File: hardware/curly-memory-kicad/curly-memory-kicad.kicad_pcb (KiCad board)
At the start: 2 copper layers, 30 x 100.5 mm, 138 parts, among them J101 Conn_01x05, J102 Conn_01x05, J103 Conn_01x01_Male, J104 Conn_01x01_Male, J105 Conn_01x01_Male, J106 Conn_01x01_Male, J107 AudioJack2, J201 AudioJack2, J202 AudioJack2, J203 AudioJack2, J204 Conn_01x01_Male, J205 Conn_01x01_Male, J206 Conn_01x01_Male, J207 Conn_01x01_Male, J301 Conn_01x01_Male, J302 Conn_01x01_Male, J303 Conn_01x01_Male, J304 Conn_01x01_Male, J305 AudioJack2, J306 AudioJack2, J307 AudioJack2, J308 AudioJack2, J501 Conn_02x05_Odd_Even, SW101 FSM, SW102 FSM, SW401 FSM, SW402 FSM, U101 MCP3008-I/SL, U102 ESP32-WROOM-32, U103 MCP4822-E/SN, U104 MCP4822-E/SN, U105 MCP42010-E/SL, U106 MCP42010-E/SL, U107 MCP6004, U201 MCP6004, U301 MCP6004, U501 NCP1117-5.0_SOT223, U502 NCP1117-3.3_SOT223

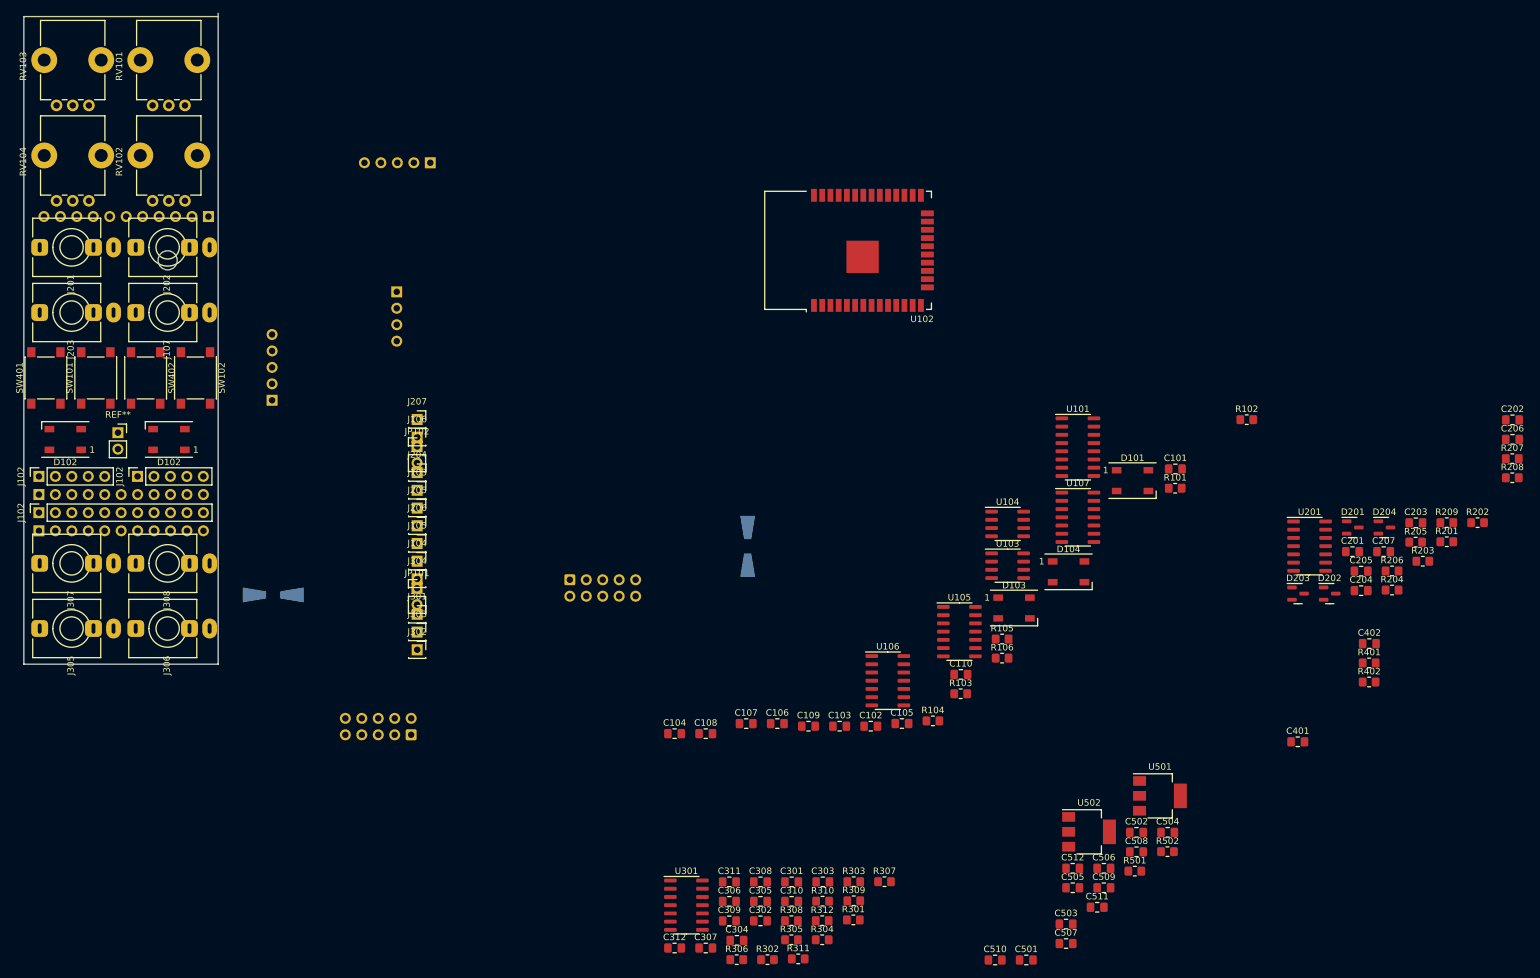
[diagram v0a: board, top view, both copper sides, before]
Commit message: all components placed on the main board
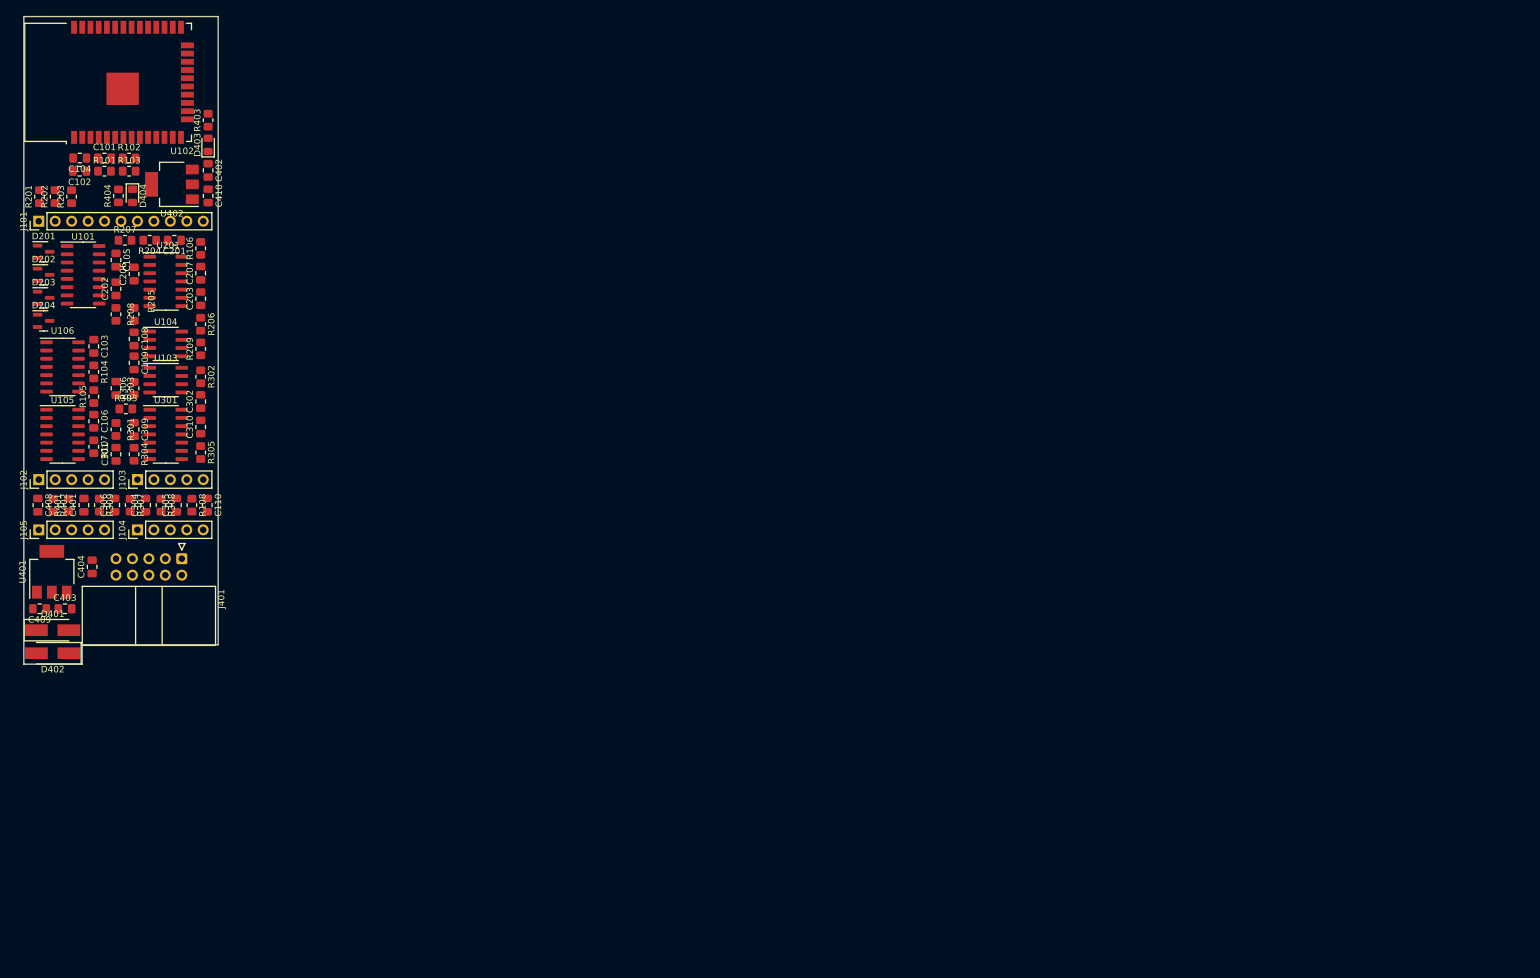
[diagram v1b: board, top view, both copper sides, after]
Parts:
- removed C107, C204, C205, C307, C308, C502, C503, C504, C509, C510: 1uF, Capacitor_SMD:C_0805_2012Metric_Pad1.18x1.45mm_HandSolder
- removed C311, C312, C501, C505, C506, C507, C508, C511, C512: 100nF, Capacitor_SMD:C_0805_2012Metric_Pad1.18x1.45mm_HandSolder
- removed D101, D102 (x2), D103, D104: WS2812B, LED_SMD:LED_WS2812B_PLCC4_5.0x5.0mm_P3.2mm
- removed D501, D502: S1A, Diode_SMD:D_SMA-SMB_Universal_Handsoldering
- removed the J101 at (28.5, 30.9)
- removed the J101 at (38.3, 59.2)
- removed the J102 at (17.6, 71.0)
- removed the J102 at (2.33, 76.6)
- removed the J102 at (2.33, 71.0)
- removed the J102 at (2.33, 79.4)
- removed the J102 at (2.33, 73.8)
- removed the J102 at (62.8, 22.6)
- removed J106, J204, J205, J206, J207, J301, J302, J303, J304: Conn_01x01_Male, Connector_PinSocket_2.54mm:PinSocket_1x01_P2.54mm_Vertical
- removed J107, J201, J202, J203, J305, J306, J307, J308: AudioJack2, AudioJacks:Jack_3.5mm_QingPu_WQP-PJ398SM_Vertical
- removed J501: Conn_02x05_Odd_Even, Connector_IDC:IDC-Header_2x05_P2.54mm_Vertical
- removed JP101, JP102: Jumper_2_Open, Connector_PinHeader_2.54mm:PinHeader_1x02_P2.54mm_Vertical
- removed R310, R311, R312, R501: 100K, Resistor_SMD:R_0805_2012Metric_Pad1.20x1.40mm_HandSolder
- removed R502: 56k, Resistor_SMD:R_0805_2012Metric_Pad1.20x1.40mm_HandSolder
- removed REF**: PinSocket_1x02_P2.54mm_Vertical, Connector_PinSocket_2.54mm:PinSocket_1x02_P2.54mm_Vertical
- removed REF**: IDC-Header_2x05_P2.54mm_Horizontal, Connector_IDC:IDC-Header_2x05_P2.54mm_Horizontal
- removed REF**: PinSocket_1x04_P2.54mm_Vertical, Connector_PinSocket_2.54mm:PinSocket_1x04_P2.54mm_Vertical
- removed RV101, RV102, RV103, RV104: PTV09A-4225F-B203, Potentiometer_THT:Potentiometer_Bourns_PTV09A-1_Single_Vertical
- removed SW101, SW102, SW401, SW402: FSM, Button_Switch_SMD:SW_Push_1P1T_NO_6x6mm_H9.5mm
- removed U107: MCP6004, Package_SO:SOIC-14_3.9x8.7mm_P1.27mm
- removed U501: NCP1117-5.0_SOT223, Package_TO_SOT_SMD:SOT-223-3_TabPin2
- removed U502: NCP1117-3.3_SOT223, Package_TO_SOT_SMD:SOT-223-3_TabPin2
- added C403: 10uF, Capacitor_SMD:C_0805_2012Metric_Pad1.18x1.45mm_HandSolder, F.Cu at (6.35, 91.4)
- added C404: 10uF, Capacitor_SMD:C_0805_2012Metric_Pad1.18x1.45mm_HandSolder, F.Cu at (10.5, 85.0)
- added C408: 100nF, Capacitor_SMD:C_0805_2012Metric_Pad1.18x1.45mm_HandSolder, F.Cu at (2.16, 75.4)
- added C409: 10uF, Capacitor_SMD:C_0805_2012Metric_Pad1.18x1.45mm_HandSolder, F.Cu at (2.43, 91.4)
- added C410: 10uF, Capacitor_SMD:C_0805_2012Metric_Pad1.18x1.45mm_HandSolder, F.Cu at (28.4, 27.7)
- added D401: S1A, Diode_SMD:D_SMA_Handsoldering, F.Cu at (4.45, 94.7)
- added D402: S1A, Diode_SMD:D_SMA_Handsoldering, F.Cu at (4.45, 98.3)
- added D403: LED, LED_SMD:LED_0805_2012Metric_Pad1.15x1.40mm_HandSolder, F.Cu at (28.4, 19.8)
- added D404: LED, LED_SMD:LED_0805_2012Metric_Pad1.15x1.40mm_HandSolder, F.Cu at (16.8, 27.7)
- added J101: Conn_01x11, Connector_PinHeader_2.54mm:PinHeader_1x11_P2.54mm_Vertical, F.Cu at (2.30, 31.6)
- added J102: Conn_01x05, Connector_PinHeader_2.54mm:PinHeader_1x05_P2.54mm_Vertical, F.Cu at (2.30, 71.5)
- added J401: Conn_02x05_Odd_Even, Connector_IDC:IDC-Header_2x05_P2.54mm_Horizontal, F.Cu at (24.4, 83.7)
- added R107: 100R, Resistor_SMD:R_0805_2012Metric_Pad1.20x1.40mm_HandSolder, F.Cu at (10.8, 66.4)
- added R108: 100K, Resistor_SMD:R_0805_2012Metric_Pad1.20x1.40mm_HandSolder, F.Cu at (25.9, 75.4)
- added R403: 150R, Resistor_SMD:R_0805_2012Metric_Pad1.20x1.40mm_HandSolder, F.Cu at (28.4, 16.0)
- added R404: 150R, Resistor_SMD:R_0805_2012Metric_Pad1.20x1.40mm_HandSolder, F.Cu at (14.6, 27.7)
- added U401: NCP1117-5.0_SOT223, Package_TO_SOT_SMD:SOT-223-3_TabPin2, F.Cu at (4.32, 85.7)
- added U402: NCP1117-3.3_SOT223, Package_TO_SOT_SMD:SOT-223-3_TabPin2, F.Cu at (22.9, 25.9)
- C103, C106, C309, C310: value 1uF -> 100nF
- C304: value 22pF -> 1uF
- C402: value 100nF -> 10uF
- J103, J104, J105: value Conn_01x01_Male -> Conn_01x05; footprint Connector_PinSocket_2.54mm:PinSocket_1x01_P2.54mm_Vertical -> Connector_PinHeader_2.54mm:PinHeader_1x05_P2.54mm_Vertical
- R105: value 100R -> 1K
- R106: value 100K -> 1K
- R304: value 47k -> 100K
- R401: value 1K -> 100K
- R402: value 1K -> 56k
- moved R202 225.3 mm to (4.83, 27.8), turned to 90 degrees
- moved R201 223.7 mm to (2.41, 27.8), turned to 90 degrees
- moved R208 217.1 mm to (14.2, 46.0), turned to -90 degrees
- moved R207 216.8 mm to (15.6, 34.5)
- moved C202 216.6 mm to (14.2, 42.0), turned to 90 degrees
- moved R203 216.1 mm to (7.37, 27.8), turned to 90 degrees
- moved C206 214.4 mm to (17.0, 39.8), turned to 90 degrees
- moved D204 209.5 mm to (3.05, 47.0)
- moved D201 206.6 mm to (3.05, 36.3)
- moved R402 205.0 mm to (4.54, 75.4), turned to -90 degrees
- moved D202 204.6 mm to (3.05, 39.9)
- moved R401 202.3 mm to (6.89, 75.4), turned to 90 degrees
- moved R205 201.0 mm to (17.0, 46.0), turned to -90 degrees
- moved R204 199.3 mm to (19.4, 34.5), turned to 180 degrees
- moved D203 199.0 mm to (3.05, 43.4)
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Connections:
- C102 pad 1: +5V -> +3V3
- C103 pad 1: +3V3 -> +5V
- C104 pad 1: +5V -> +3V3
- C105 pad 1: +3V3 -> +5V
- C110 pad 2: Net-(C110-Pad2) -> /DRY_WET
- C304 pad 1: Net-(C304-Pad1) -> /output/OUT_1_OUT
- C304 pad 2: Net-(C304-Pad2) -> Net-(C301-Pad1)
- C305 pad 1: /output/OUT_1 -> /output/OUT_2_OUT
- C305 pad 2: Net-(C301-Pad1) -> Net-(C302-Pad1)
- C306 pad 1: /output/OUT_2 -> /output/OUT_0_OUT
- C306 pad 2: Net-(C302-Pad1) -> Net-(C303-Pad1)
- C401 pad 1: GND -> +5V
- C402 pad 1: GND -> +5V
- J103 pad 1: /RES0_A1 -> Net-(J103-Pad1)
- J104 pad 1: /RES0_W1 -> /output/OUT_0_OUT
- J105 pad 1: GND -> /RES0_A1
- R102 pad 1: /RES1_W0 -> +3V3
- R102 pad 2: Net-(R102-Pad2) -> /SW_1
- R103 pad 1: /RES1_W1 -> +3V3
- R103 pad 2: Net-(R102-Pad2) -> /SW_0
- R104 pad 1: Net-(R102-Pad2) -> /RES1_W0
- R105 pad 1: Net-(R104-Pad2) -> /RES1_W1
- R105 pad 2: /RES0_A1 -> Net-(R104-Pad2)
- R106 pad 1: GND -> Net-(R104-Pad2)
- R106 pad 2: Net-(C110-Pad2) -> Net-(R106-Pad2)
- R201 pad 1: Net-(J201-PadS) -> /input/IN_0_IN+
- R202 pad 1: Net-(J202-PadS) -> /input/IN_1_IN+
- R203 pad 1: Net-(J203-PadS) -> /input/IN_2_IN+
- R303 pad 1: /output/OUT_3+ -> /output/OUT_0+
- R304 pad 1: /output/OUT_0+ -> Net-(C301-Pad2)
- R304 pad 2: Net-(C304-Pad2) -> Net-(C301-Pad1)
- R305 pad 1: Net-(C301-Pad2) -> Net-(C302-Pad2)
- R305 pad 2: Net-(C301-Pad1) -> Net-(C302-Pad1)
- R306 pad 1: Net-(C302-Pad2) -> Net-(C303-Pad2)
- R306 pad 2: Net-(C302-Pad1) -> Net-(C303-Pad1)
- R307 pad 1: Net-(C303-Pad2) -> GND
- R307 pad 2: Net-(C303-Pad1) -> /output/OUT_1_OUT
- R308 pad 1: Net-(C304-Pad2) -> GND
- R308 pad 2: Net-(C304-Pad1) -> /output/OUT_2_OUT
- R309 pad 2: /output/OUT_1 -> /output/OUT_0_OUT
- R401 pad 1: +3V3 -> +5V
- R401 pad 2: /SW_0 -> V_OFFSET
- R402 pad 1: +3V3 -> V_OFFSET
- R402 pad 2: /SW_1 -> GND
- U102 pad 10: Net-(J102-Pad5) -> unconnected-(U102-Pad10)
- U102 pad 24: Net-(J102-Pad1) -> unconnected-(U102-Pad24)
- U102 pad 28: Net-(J102-Pad2) -> Net-(J103-Pad1)
- U102 pad 33: Net-(J102-Pad3) -> unconnected-(U102-Pad33)
- U102 pad 36: Net-(J102-Pad4) -> unconnected-(U102-Pad36)
- U102 pad 8: unconnected-(U102-Pad8) -> Net-(U102-Pad8)
- U201 pad 12: (no net) -> GND
- U201 pad 13: (no net) -> Net-(R104-Pad2)
- U201 pad 14: (no net) -> Net-(R106-Pad2)
- U301 pad 1: Net-(C304-Pad1) -> Net-(C303-Pad1)
- U301 pad 12: GND -> unconnected-(U301-Pad12)
- U301 pad 13: Net-(C303-Pad2) -> unconnected-(U301-Pad13)
- U301 pad 14: Net-(C303-Pad1) -> unconnected-(U301-Pad14)
- U301 pad 2: Net-(C304-Pad2) -> Net-(C303-Pad2)
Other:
- board size 30 x 100.5 mm -> 30 x 100 mm

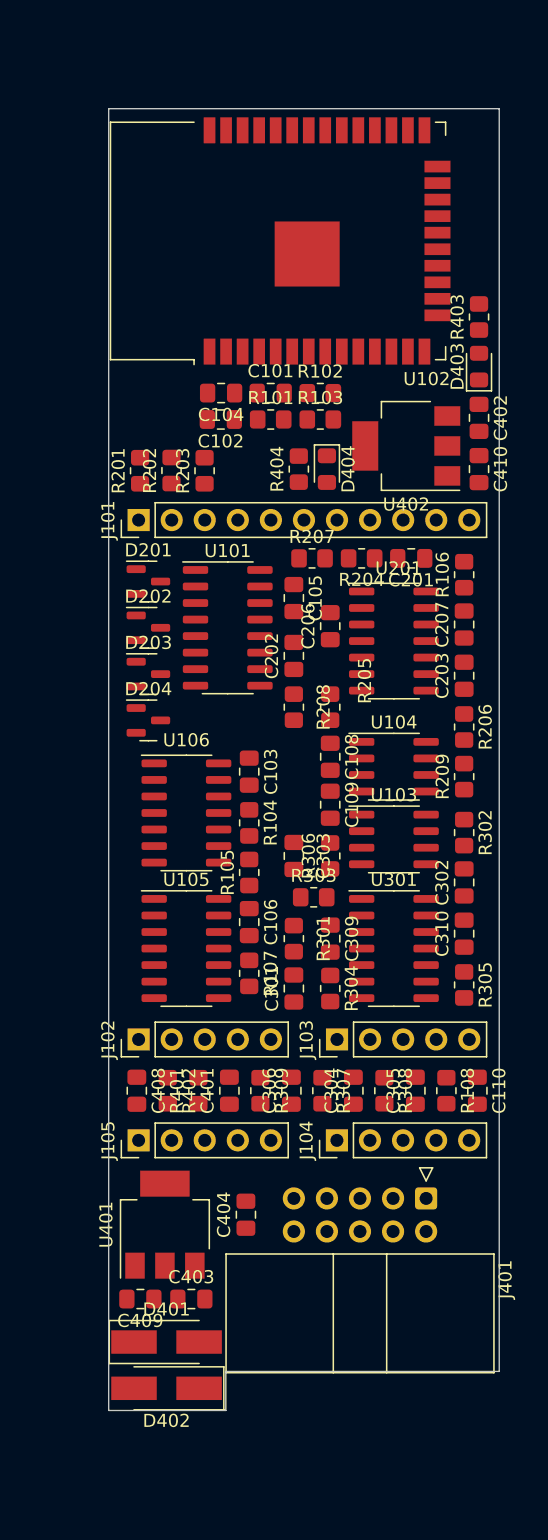
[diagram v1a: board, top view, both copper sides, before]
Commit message: more pcb tracked
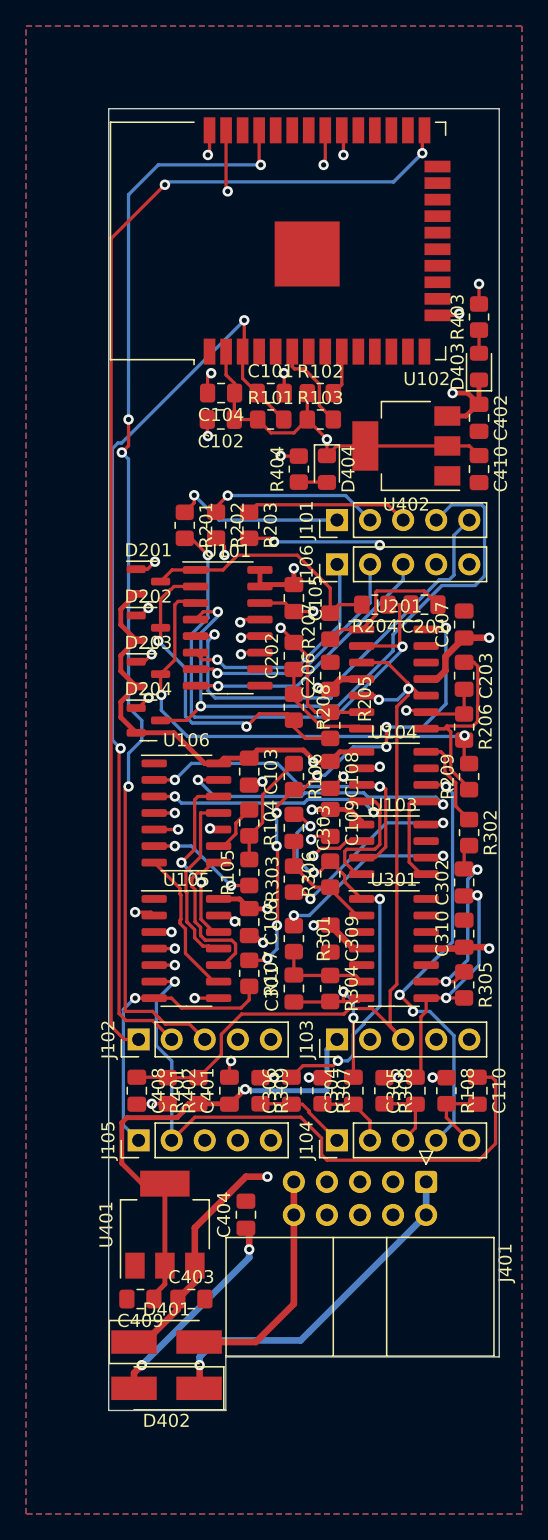
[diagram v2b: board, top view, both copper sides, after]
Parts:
- added J106: Conn_01x05, Connector_PinHeader_2.54mm:PinHeader_1x05_P2.54mm_Vertical, F.Cu at (17.5, 35.0)
- J101: value Conn_01x11 -> Conn_01x06; footprint Connector_PinHeader_2.54mm:PinHeader_1x11_P2.54mm_Vertical -> Connector_PinHeader_2.54mm:PinHeader_1x05_P2.54mm_Vertical
- moved R106 20.3 mm to (14.2, 51.3), turned to -90 degrees
- moved J101 15.2 mm to (17.5, 31.6)
- moved R201 5.42 mm to (5.84, 32.0), turned to -90 degrees
- moved R202 5.42 mm to (8.26, 32.0), turned to -90 degrees
- moved R203 5.42 mm to (10.8, 32.0), turned to -90 degrees
- moved R207 5.39 mm to (17.0, 39.8), turned to 90 degrees
- moved C206 3.81 mm to (17.0, 43.6)
- moved C201 3.70 mm to (24.3, 38.1)
- moved R204 3.70 mm to (20.4, 38.1)
- moved U201 2.92 mm to (21.9, 43.8)
- moved C303 2.16 mm to (14.2, 55.2)
- moved R303 2.07 mm to (14.2, 59.2), turned to 90 degrees
- moved R205 1.40 mm to (17.0, 47.4)
- moved C108 1.40 mm to (17.0, 51.2)
- moved C109 1.40 mm to (17.0, 54.9)
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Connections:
- J103 pad 1: Net-(J103-Pad1) -> +5V
- J103 pad 2: Net-(U102-Pad8) -> +3V3
- J103 pad 4: +3V3 -> Net-(J103-Pad4)
- J103 pad 5: +5V -> Net-(U102-Pad33)
- U102 pad 10: unconnected-(U102-Pad10) -> /RES_~SHDN
- U102 pad 11: unconnected-(U102-Pad11) -> /RES_~RS
- U102 pad 28: Net-(J103-Pad1) -> /SPI2_CS_2
- U102 pad 33: unconnected-(U102-Pad33) -> Net-(U102-Pad33)
- U102 pad 8: Net-(U102-Pad8) -> Net-(J103-Pad4)
- U104 pad 2: /SPI3_CS_1 -> /SPI2_CS_1
- U104 pad 3: /SPI3_CLK -> /SPI2_CLK
- U104 pad 4: /SPI3_MOSI -> /SPI2_MOSI
- U104 pad 5: /SPI3_MISO -> /SPI2_MISO
- U105 pad 1: /SPI2_CS_1 -> /SPI3_CS_1
- U105 pad 13: /SPI2_MISO -> /SPI3_MISO
- U105 pad 2: /SPI2_CLK -> /SPI3_CLK
- U105 pad 3: /SPI2_MOSI -> /SPI3_MOSI
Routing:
- net +5V: track 0.00 -> 161.7 mm, vias 0 -> 6
- net -12V: track 0.00 -> 93.0 mm, vias 0 -> 4
- net +3V3: track 0.00 -> 91.6 mm, vias 0 -> 1
- net /BOOT: track 0.00 -> 91.5 mm, vias 0 -> 2
- net /SPI3_MISO: track 0.00 -> 85.1 mm, vias 0 -> 3
- net /PROG_TX: track 0.00 -> 84.9 mm, vias 0 -> 4
- net /SPI3_MOSI: track 0.00 -> 83.4 mm, vias 0 -> 3
- net /SPI3_CLK: track 0.00 -> 80.2 mm, vias 0 -> 3
- net /RST: track 0.00 -> 71.8 mm, vias 0 -> 2
- net +12V: track 0.00 -> 66.5 mm, vias 0 -> 3
- net V_OFFSET: track 0.00 -> 63.1 mm, vias 0 -> 2
- net /IN_3: track 0.00 -> 49.5 mm, vias 0 -> 2
- net /RES0_W1: track 0.00 -> 49.5 mm, vias 0 -> 1
- net GND: track 0.00 -> 44.0 mm, vias 0 -> 28
- net Net-(C201-Pad2): track 0.00 -> 41.5 mm, vias 0 -> 2
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- added copper zone on B.Cu, net GND
- added copper zone on F.Cu, net GND
- added copper zone on In1.Cu, net GND
- added copper zone on In2.Cu, net GND
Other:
- outline, holes or cut-outs redrawn
- copper layers 2 -> 4

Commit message: more pcb tracked- again
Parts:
- moved C109 0.05 mm to (17.0, 54.9)
- moved C108 0.05 mm to (17.0, 51.1)
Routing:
- net Net-(J103-Pad5): track 0.00 -> 87.9 mm, vias 0 -> 2
- net /PROG_RX: track 0.00 -> 81.2 mm, vias 0 -> 4
- net /SPI3_CS_1: track 0.00 -> 78.5 mm, vias 0 -> 2
- net /LEDS: track 0.00 -> 77.4 mm, vias 0 -> 2
- net /RES_~SHDN: track 14.0 -> 88.1 mm, vias 2 -> 6
- net Net-(J103-Pad4): track 0.00 -> 69.7 mm, vias 0 -> 1
- net /SPI2_CS_0: track 4.92 -> 69.4 mm, vias 1 -> 6
- net /SPI2_CS_1: track 1.45 -> 63.2 mm, vias 1 -> 4
- net /SPI2_CS_2: track 0.00 -> 59.1 mm, vias 0 -> 4
- net /RES_~RS: track 13.3 -> 70.4 mm, vias 0 -> 2
- net /SPI2_MOSI: track 28.0 -> 81.7 mm, vias 2 -> 3
- net /SPI3_CS_0: track 0.00 -> 52.5 mm, vias 0 -> 3
- net /SPI2_MISO: track 30.4 -> 75.6 mm, vias 2 -> 3
- net /SPI2_CLK: track 27.5 -> 71.4 mm, vias 2 -> 3
- net /IN_0: track 32.1 -> 67.5 mm, vias 0 -> 2
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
